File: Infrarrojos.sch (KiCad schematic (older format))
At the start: 12 parts, among them P13 CONN_01X04, P14 CONN_01X04, U11 40106

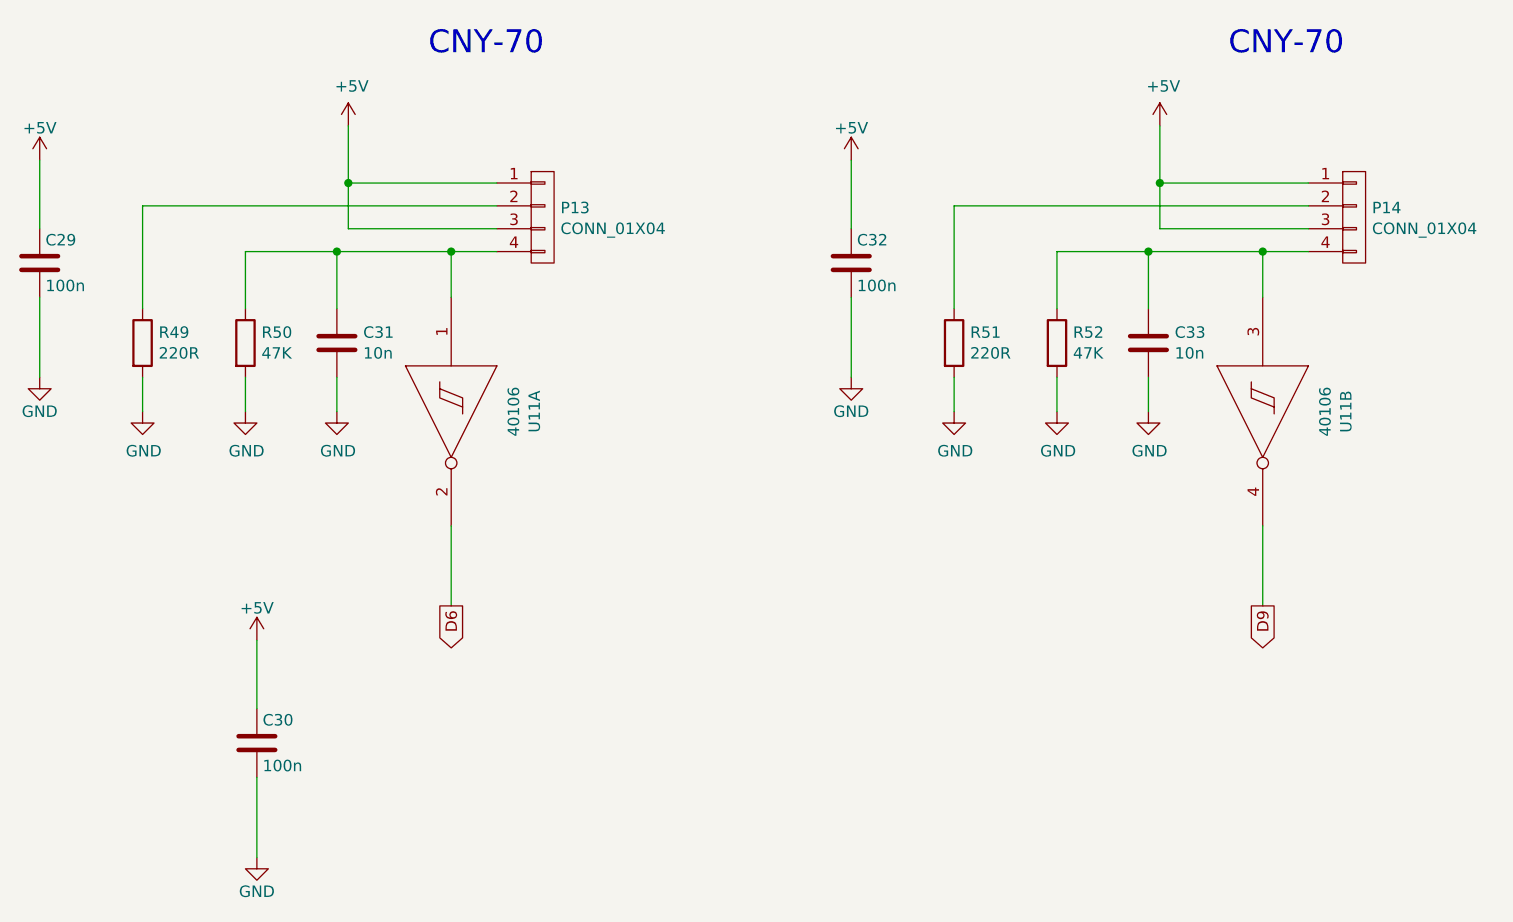
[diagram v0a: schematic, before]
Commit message: asignacion inicial de huellas
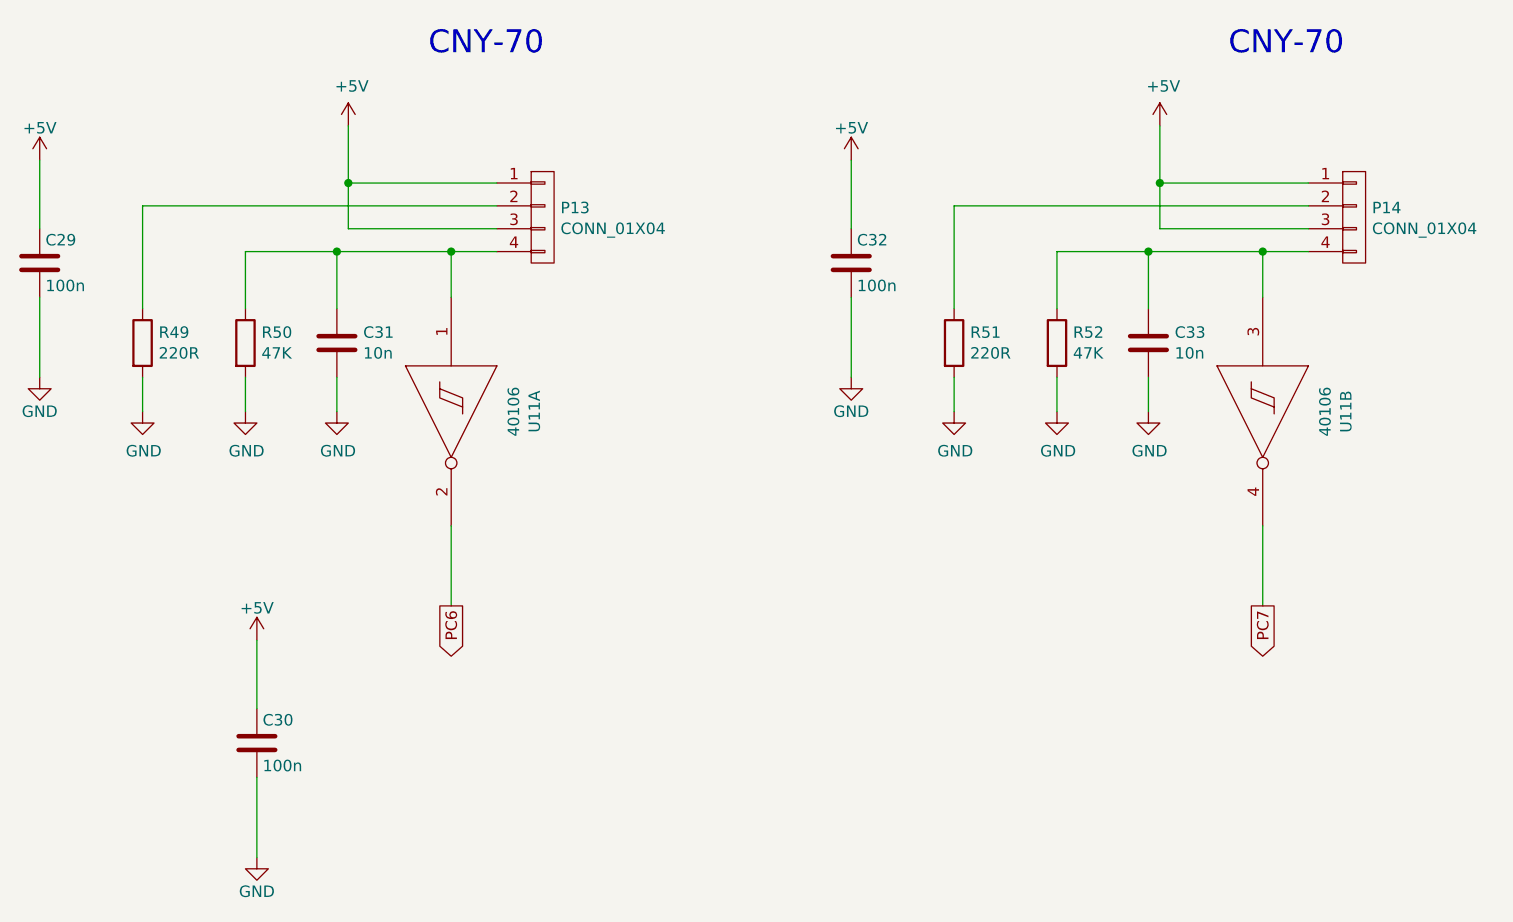
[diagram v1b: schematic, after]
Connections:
- net D6 renamed PC6
- net D9 renamed PC7
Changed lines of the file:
@@
 $EndComp
 $Comp
-L GND #PWR87
+L GND #PWR0105
 U 1 1 588EB566
 P 950 2550
-F 0 "#PWR87" H 950 2300 50  0001 C CNN
+F 0 "#PWR0105" H 950 2300 50  0001 C CNN
 F 1 "GND" H 950 2400 50  0000 C CNN
 F 2 "" H 950 2550 50  0000 C CNN
@@
 $EndComp
 $Comp
-L +5V #PWR86
+L +5V #PWR0106
 U 1 1 588EB567
 P 950 1600
-F 0 "#PWR86" H 950 1450 50  0001 C CNN
+F 0 "#PWR0106" H 950 1450 50  0001 C CNN
 F 1 "+5V" H 950 1740 50  0000 C CNN
 F 2 "" H 950 1600 50  0000 C CNN
@@
 $EndComp
 $Comp
-L GND #PWR88
+L GND #PWR0107
 U 1 1 588EB56B
 P 1400 2700
-F 0 "#PWR88" H 1400 2450 50  0001 C CNN
+F 0 "#PWR0107" H 1400 2450 50  0001 C CNN
 F 1 "GND" H 1405 2527 50  0000 C CNN
 F 2 "" H 1400 2700 50  0000 C CNN
@@
 $EndComp
 $Comp
-L GND #PWR89
+L GND #PWR0108
 U 1 1 588EB56C
 P 1850 2700
-F 0 "#PWR89" H 1850 2450 50  0001 C CNN
+F 0 "#PWR0108" H 1850 2450 50  0001 C CNN
 F 1 "GND" H 1855 2527 50  0000 C CNN
 F 2 "" H 1850 2700 50  0000 C CNN
@@
 $EndComp
 $Comp
-L GND #PWR92
+L GND #PWR0109
 U 1 1 588EB56D
 P 2250 2700
-F 0 "#PWR92" H 2250 2450 50  0001 C CNN
+F 0 "#PWR0109" H 2250 2450 50  0001 C CNN
 F 1 "GND" H 2255 2527 50  0000 C CNN
 F 2 "" H 2250 2700 50  0000 C CNN
@@
 $EndComp
 $Comp
-L +5V #PWR93
+L +5V #PWR0110
 U 1 1 588EB56F
 P 2300 1450
-F 0 "#PWR93" H 2300 1300 50  0001 C CNN
+F 0 "#PWR0110" H 2300 1300 50  0001 C CNN
 F 1 "+5V" H 2315 1623 50  0000 C CNN
 F 2 "" H 2300 1450 50  0000 C CNN
@@
 $EndComp
 $Comp
-L GND #PWR95
+L GND #PWR0111
 U 1 1 588EB572
 P 4500 2550
-F 0 "#PWR95" H 4500 2300 50  0001 C CNN
+F 0 "#PWR0111" H 4500 2300 50  0001 C CNN
 F 1 "GND" H 4500 2400 50  0000 C CNN
 F 2 "" H 4500 2550 50  0000 C CNN
@@
 $EndComp
 $Comp
-L +5V #PWR94
+L +5V #PWR0112
 U 1 1 588EB573
 P 4500 1600
-F 0 "#PWR94" H 4500 1450 50  0001 C CNN
+F 0 "#PWR0112" H 4500 1450 50  0001 C CNN
 F 1 "+5V" H 4500 1740 50  0000 C CNN
 F 2 "" H 4500 1600 50  0000 C CNN
@@
 $EndComp
 $Comp
-L GND #PWR96
+L GND #PWR0113
 U 1 1 588EB577
 P 4950 2700
-F 0 "#PWR96" H 4950 2450 50  0001 C CNN
+F 0 "#PWR0113" H 4950 2450 50  0001 C CNN
 F 1 "GND" H 4955 2527 50  0000 C CNN
 F 2 "" H 4950 2700 50  0000 C CNN
@@
 $EndComp
 $Comp
-L GND #PWR97
+L GND #PWR0114
 U 1 1 588EB578
 P 5400 2700
-F 0 "#PWR97" H 5400 2450 50  0001 C CNN
+F 0 "#PWR0114" H 5400 2450 50  0001 C CNN
 F 1 "GND" H 5405 2527 50  0000 C CNN
 F 2 "" H 5400 2700 50  0000 C CNN
@@
 $EndComp
 $Comp
-L GND #PWR98
+L GND #PWR0115
 U 1 1 588EB579
 P 5800 2700
-F 0 "#PWR98" H 5800 2450 50  0001 C CNN
+F 0 "#PWR0115" H 5800 2450 50  0001 C CNN
 F 1 "GND" H 5805 2527 50  0000 C CNN
 F 2 "" H 5800 2700 50  0000 C CNN
@@
 $EndComp
 $Comp
-L +5V #PWR99
+L +5V #PWR0116
 U 1 1 588EB57B
 P 5850 1450
-F 0 "#PWR99" H 5850 1300 50  0001 C CNN
+F 0 "#PWR0116" H 5850 1300 50  0001 C CNN
 F 1 "+5V" H 5865 1623 50  0000 C CNN
 F 2 "" H 5850 1450 50  0000 C CNN
@@
 Connection ~ 6300 2000
 Text GLabel 6300 3550 3    50   Output ~ 0
-D9
+PC7
 Wire Wire Line
 	6300 3550 6300 3200
 Text GLabel 2750 3550 3    50   Output ~ 0
-D6
+PC6
 Wire Wire Line
 	2750 3550 2750 3200
@@
 $EndComp
 $Comp
-L GND #PWR91
+L GND #PWR0117
 U 1 1 588EB57D
 P 1900 4650
-F 0 "#PWR91" H 1900 4400 50  0001 C CNN
+F 0 "#PWR0117" H 1900 4400 50  0001 C CNN
 F 1 "GND" H 1900 4500 50  0000 C CNN
 F 2 "" H 1900 4650 50  0000 C CNN
@@
 $EndComp
 $Comp
-L +5V #PWR90
+L +5V #PWR0118
 U 1 1 588EB57E
 P 1900 3700
-F 0 "#PWR90" H 1900 3550 50  0001 C CNN
+F 0 "#PWR0118" H 1900 3550 50  0001 C CNN
 F 1 "+5V" H 1900 3840 50  0000 C CNN
 F 2 "" H 1900 3700 50  0000 C CNN

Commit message: añadida LDR. Finalizado trazado provisional
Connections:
- net PC7: now also U11.10 (Out); no longer U11.4 (Out)
- net at C33.1, P14.4 (P4), R52.1: now also U11.11 (In); no longer U11.3 (In)
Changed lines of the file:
@@
 $Descr User 8268 5846
 encoding utf-8
-Sheet 13 14
+Sheet 13 15
 Title "Detectores de infrarrojos"
-Date "2017-01-25"
+Date "2017-01-15"
 Rev "V.0.1"
 Comp "WifiPlayBoard"
@@
 $Comp
 L 40106 U11
-U 2 1 588EB570
+U 5 1 588EB570
 P 6300 2700
 F 0 "U11" H 6300 3065 50  0000 C CNN
@@
 F 8 "~" H 6300 2700 60  0001 C CNN "Provedor"
 F 9 "~" H 6300 2700 60  0001 C CNN "Ref_Proveedor"
-	2    6300 2700
+	5    6300 2700
 	0    1    1    0
 $EndComp

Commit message: actualizadas referencias en componentes y ordenado esquema electrico
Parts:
- C31, C33: Fabricante (none) -> SAMSUNG; Provedor (none) -> tme; Ref (none) -> CL21B103JBANNNC; Ref_Proveedor (none) -> CL21B103JBANNNC
- P13, P14: Fabricante (none) -> NINIGI; Provedor (none) -> tme; Ref (none) -> ZL211-40KG-S; Ref_Proveedor (none) -> ZL211-40KG-S
- R49, R51: Fabricante (none) -> YAGEO; Provedor (none) -> TME; Ref (none) -> RC0805FR-07220RL; Ref_Proveedor (none) -> RC0805FR-07220R
- R50, R52: Fabricante (none) -> VISHAY; Potencia (none) -> 1/8W; Provedor (none) -> TME; Ref (none) -> CRCW080547K0FKEA; Ref_Proveedor (none) -> CRCW080547K0FKEA; Tolerancia (none) -> 1%
- U11: Fabricante (none) -> NXP; Provedor (none) -> TME; Ref (none) -> HEF40106BT.653; Ref_Proveedor (none) -> HEF40106BT

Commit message: modificada huella de U7 a SOIC14. Corrige issue #1
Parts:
- U11: footprint Housings_SOIC:SOIC-16_3.9x9.9mm_Pitch1.27mm -> Housings_SOIC:SOIC-14_3.9x8.7mm_Pitch1.27mm
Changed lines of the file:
@@
 F 0 "U11" H 2750 3065 50  0000 C CNN
 F 1 "40106" H 2750 2974 50  0000 C CNN
-F 2 "Housings_SOIC:SOIC-16_3.9x9.9mm_Pitch1.27mm" H 2750 2700 50  0001 C CNN
+F 2 "Housings_SOIC:SOIC-14_3.9x8.7mm_Pitch1.27mm" H 2750 2700 50  0001 C CNN
 F 3 "" H 2750 2700 50  0001 C CNN
 F 4 "NXP" H 6300 2700 60  0001 C CNN "Fabricante"
@@
 F 0 "U11" H 6300 3065 50  0000 C CNN
 F 1 "40106" H 6300 2974 50  0000 C CNN
-F 2 "Housings_SOIC:SOIC-16_3.9x9.9mm_Pitch1.27mm" H 6300 2700 50  0001 C CNN
+F 2 "Housings_SOIC:SOIC-14_3.9x8.7mm_Pitch1.27mm" H 6300 2700 50  0001 C CNN
 F 3 "" H 6300 2700 50  0001 C CNN
 F 4 "NXP" H 6300 2700 60  0001 C CNN "Fabricante"
@@
 $Bitmap
 Pos 7500 4400
-Scale 0,700000
+Scale 0,000000
 Data
 89 50 4E 47 0D 0A 1A 0A 00 00 00 0D 49 48 44 52 00 00 00 EA 00 00 00 F6 08 06 00 00 00 D8 80 1B
